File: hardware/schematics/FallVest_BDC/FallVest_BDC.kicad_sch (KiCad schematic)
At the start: 8 parts, among them J1 Conn_01x02, Q1 AO3400A, U1 SIM800L-CORE, U2 ESP32-WROOM-32, U3 4554, U4 NEO-6M, U5 ICM-20948

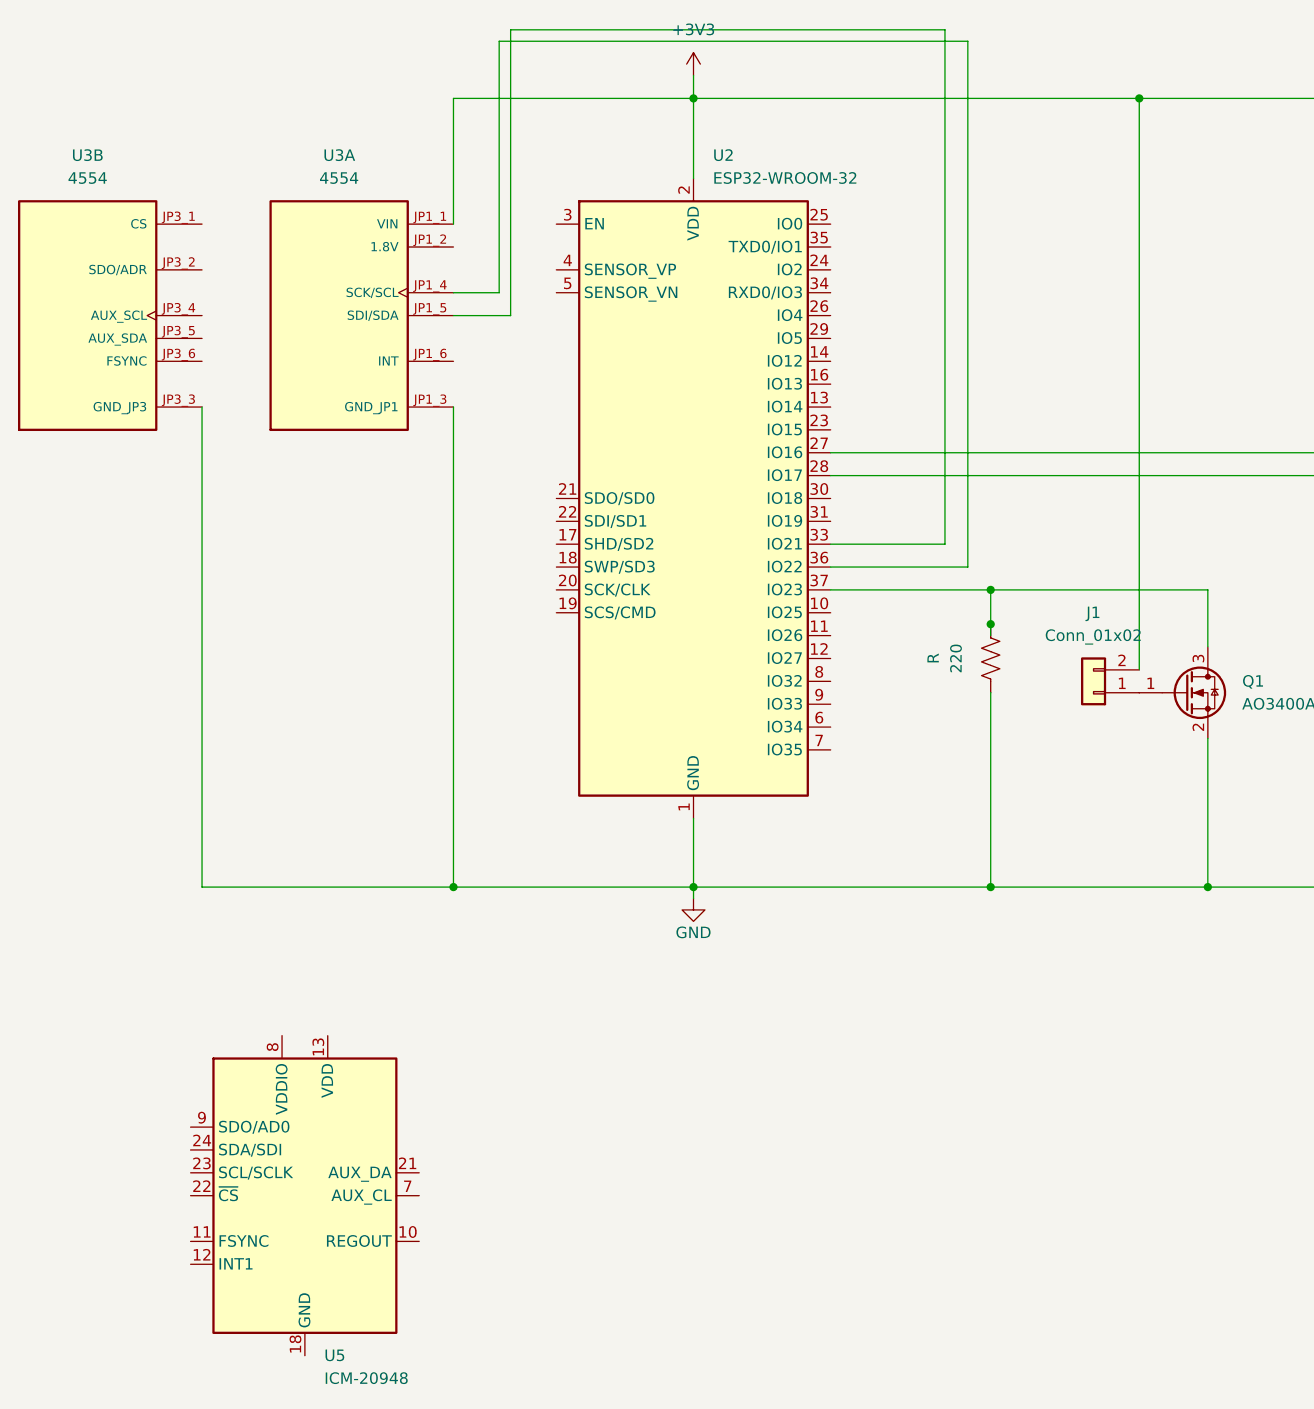
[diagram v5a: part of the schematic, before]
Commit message: Changed sensor to MPU 6050
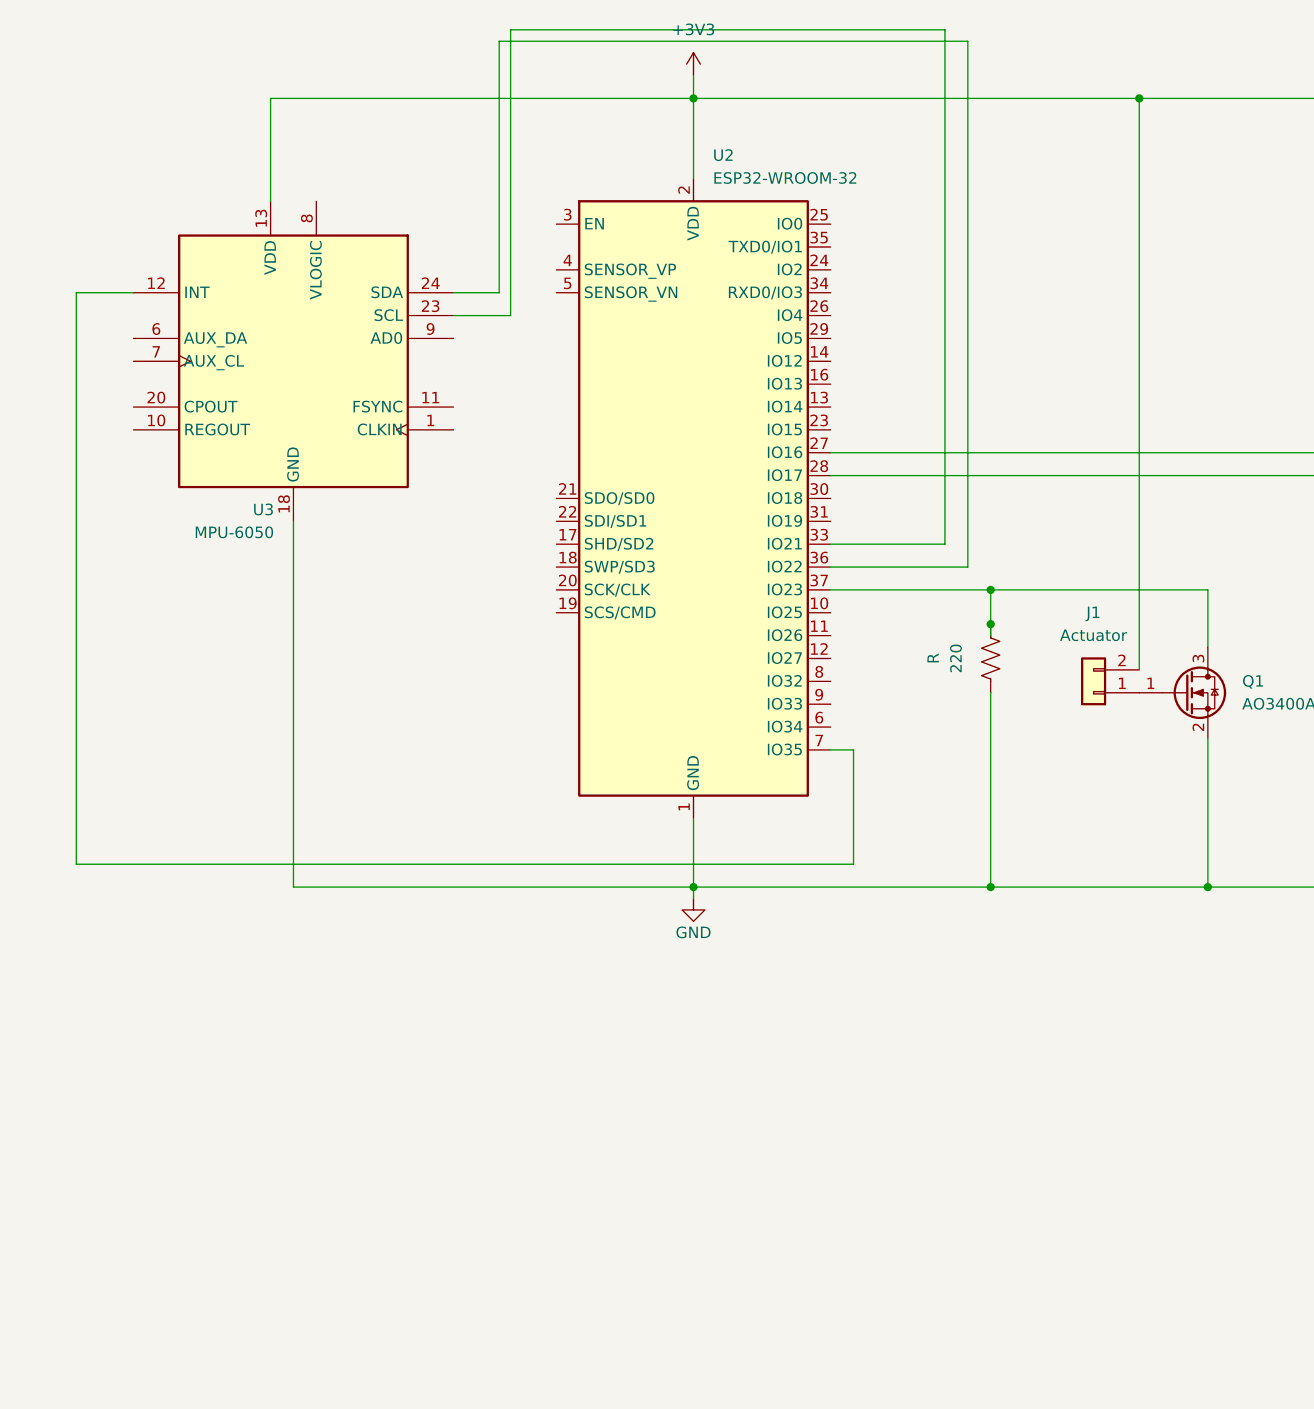
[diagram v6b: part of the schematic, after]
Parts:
- removed U3: 4554, 4554:MODULE_4554, symbol EE_VEST_SYM:4554
- removed U5: ICM-20948, Sensor_Motion:InvenSense_QFN-24_3x3mm_P0.4mm, symbol Sensor_Motion:ICM-20948
- added U3: MPU-6050, Sensor_Motion:InvenSense_QFN-24_4x4mm_P0.5mm, symbol Sensor_Motion:MPU-6050
- J1: value Conn_01x02 -> Actuator
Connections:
- net +3V3: now also U3.13 (VDD)
- net GND: now also U3.18 (GND)
- net at U2.33 (IO21): now also U3.23 (SCL)
- net at U2.36 (IO22): now also U3.24 (SDA)
- net at U2.7 (IO35): now also U3.12 (INT)

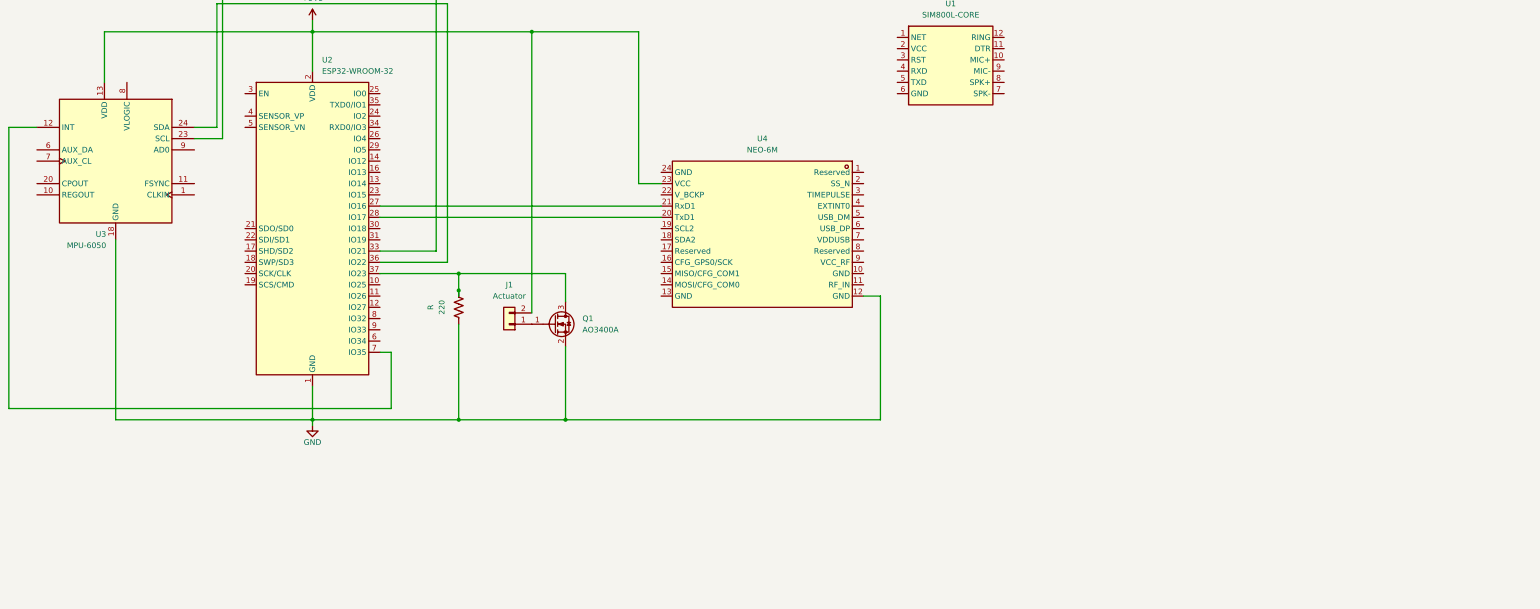
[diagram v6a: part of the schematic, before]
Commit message: Adding modules
Still need the SIM
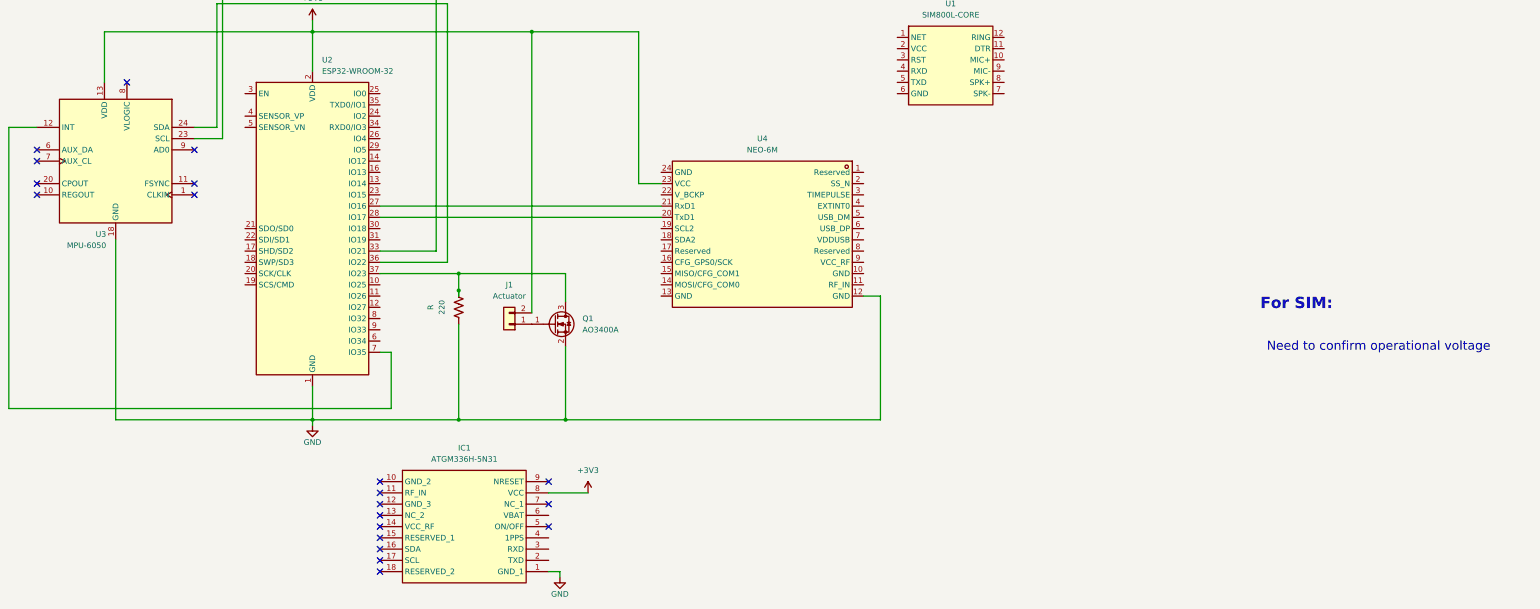
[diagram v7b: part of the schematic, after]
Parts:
- added IC1: ATGM336H-5N31, ATGM336H5N31, symbol sim800l-core:ATGM336H-5N31
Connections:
- net +3V3: now also IC1.8 (VCC)
- net GND: now also IC1.1 (GND_1)
- no-connect marks 0 -> 20
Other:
- note added: "For SIM:"
- note added: "Need to confirm operational voltage"

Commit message: Added the servo
Need to do battery and LTE
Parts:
- removed U4: NEO-6M, C2927633:GPSM-SMD_24P-L16.0-W12.2-P1.10, symbol NEO-6M:NEO-6M
- added BT1: Battery_Cell, symbol Device:Battery_Cell
- added J2: MG90S_SERVO, symbol Connector_Generic:Conn_01x03
- added R1: 220, symbol Device:R_US
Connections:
- net GND: now also J2.1 (Pin_1)
- net at U2.28 (IO17): now also IC1.2 (TXD)
- net at U2.27 (IO16): now also IC1.3 (RXD)
- net at U2.10 (IO25): now also R1.2
- new net: J2.3 (Pin_3), R1.1
- new net +5V: J2.2 (Pin_2)
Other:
- note added: "6-Axis Sensor"
- note added: "For Servo:"
- note added: "GPS"
- note added: "We can use the same 5V that we are going to use to power the ESP32 (Check whether its possible)"
- note removed: "Need to confirm operational voltage"
- moved on the sheet: IC1, R
